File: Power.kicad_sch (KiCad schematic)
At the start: 28 parts, among them U2 RT9013-33GB, U3 TPS54560DDAR

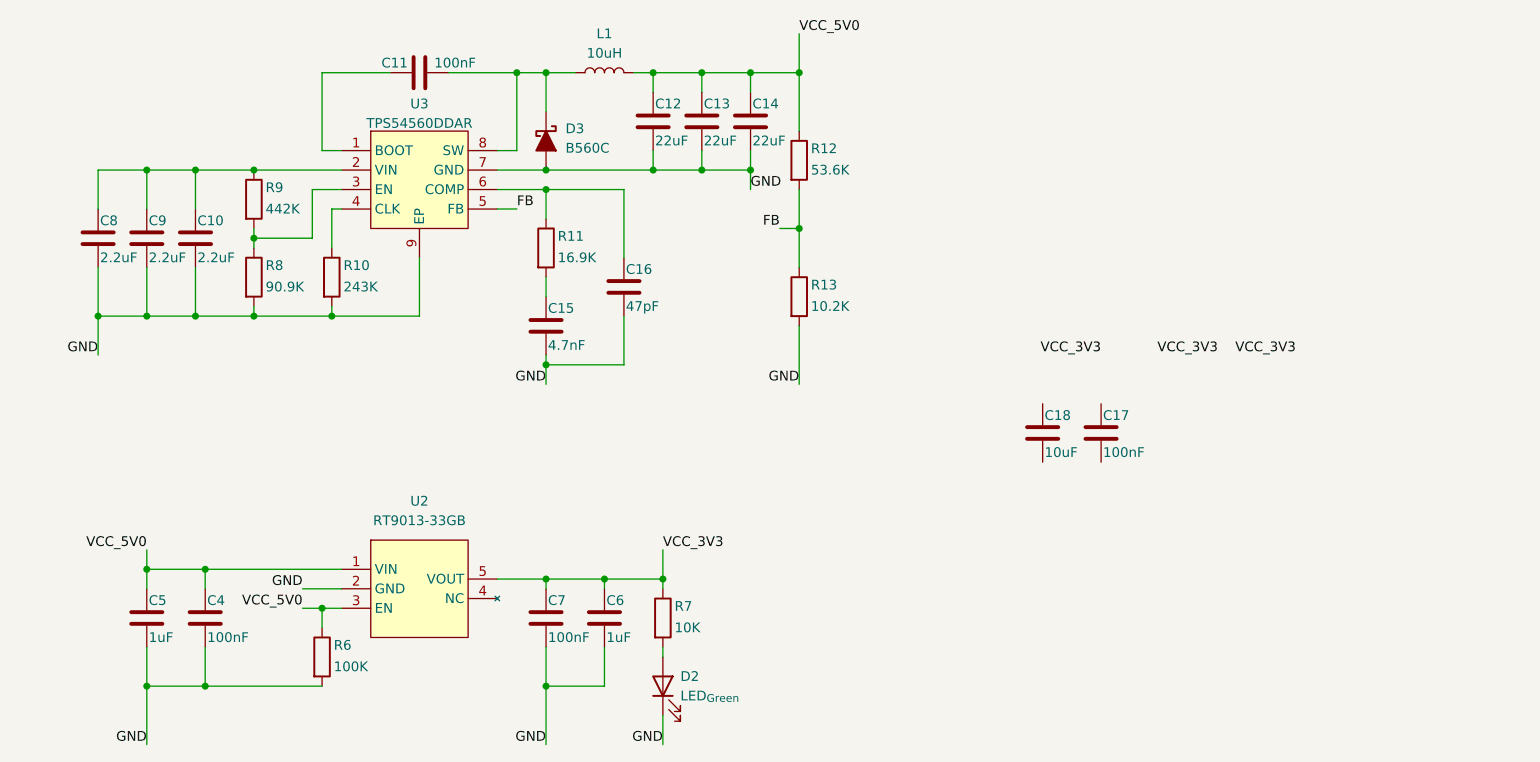
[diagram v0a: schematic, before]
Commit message: [New]: 完成整个原理图绘制和ERC检查
JIRA-ID: N/A

完成整个原理图绘制和ERC检查
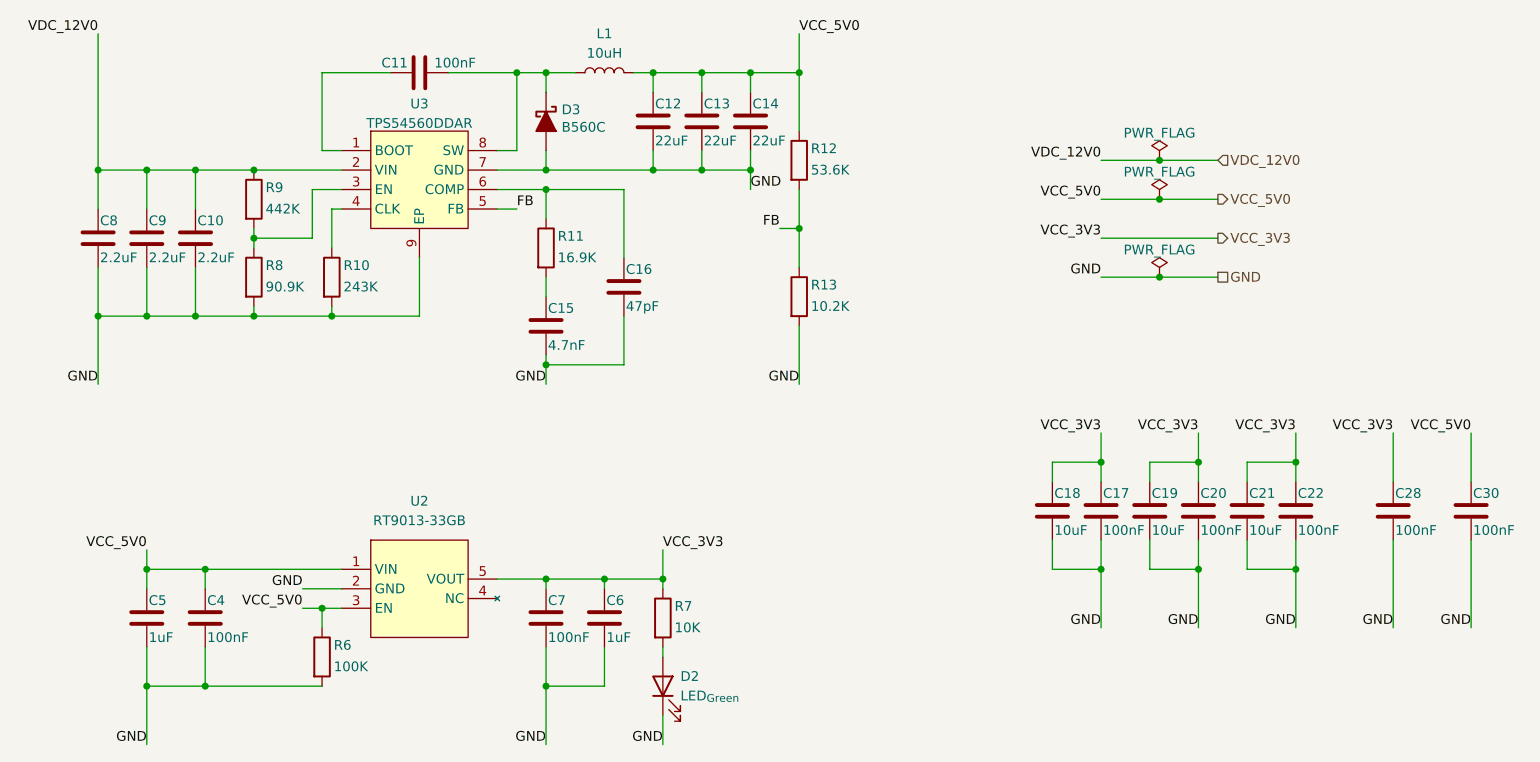
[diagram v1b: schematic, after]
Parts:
- added C19, C21: 10uF, symbol Device:C
- added C20, C22, C28, C30: 100nF, symbol Device:C
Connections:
- net GND: now also C17.2, C18.2, C19.2, C20.2, C21.2, C22.2, C28.2, C30.2
- net VCC_3V3: now also C17.1, C18.1, C19.1, C20.1, C21.1, C22.1, C28.1
- net VCC_5V0: now also C30.1
- net VDC_12V0: now reaches C10.1, C8.1, C9.1, R9.1, U3.2 (VIN)
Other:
- moved on the sheet: C17, C18, D3

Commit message: [Modify]: 完成封装的分配和PCB更新
JIRA-ID: N/A

完成封装的分配和从原理图到PCB的初始更新;完成DRC检查
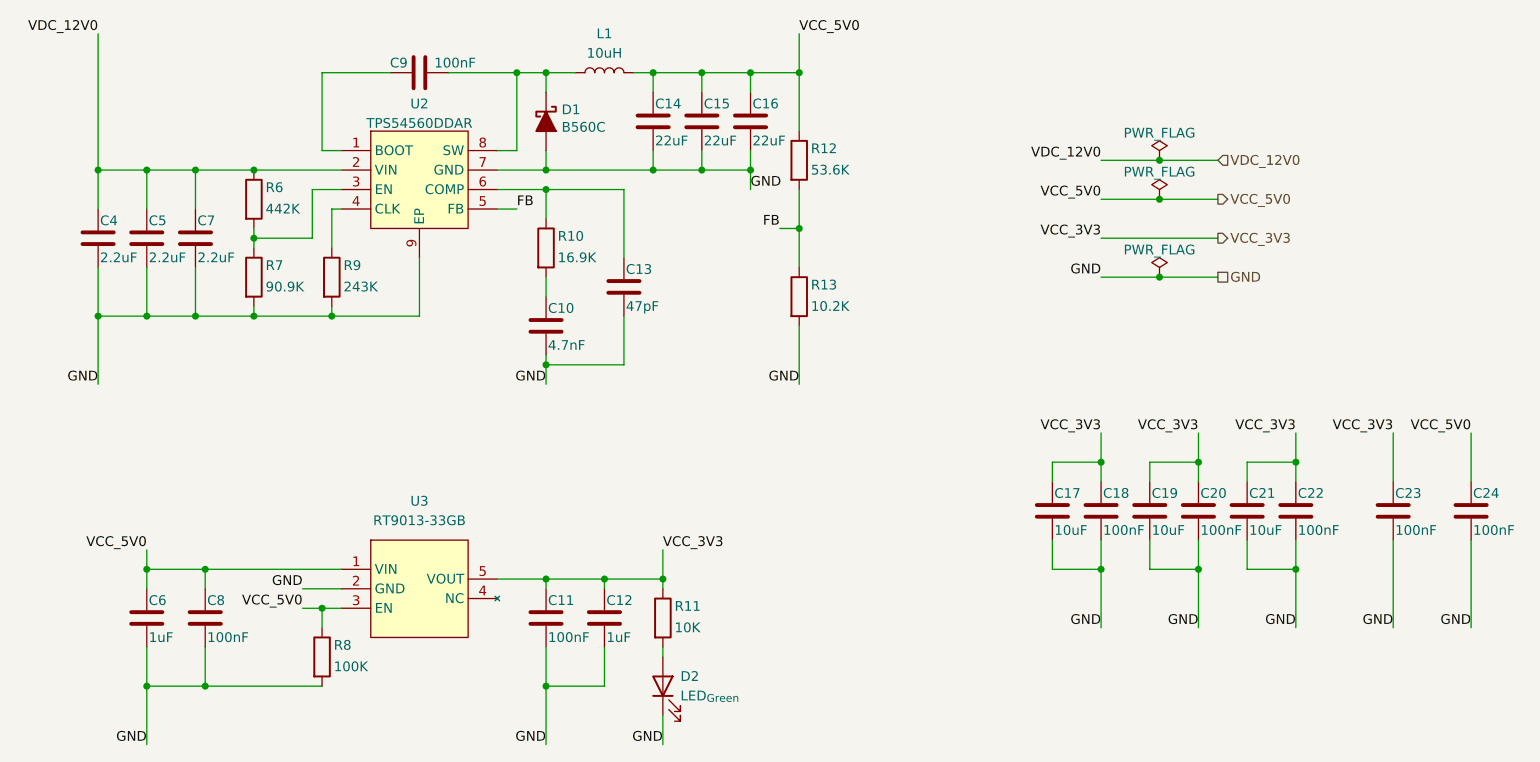
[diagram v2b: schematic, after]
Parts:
- C10: renamed from C15; footprint (none) -> Capacitor_SMD:C_0603_1608Metric
- C11: renamed from C7; footprint (none) -> Capacitor_SMD:C_0603_1608Metric
- C12: renamed from C6; footprint (none) -> Capacitor_SMD:C_0603_1608Metric
- C13: renamed from C16; footprint (none) -> Capacitor_SMD:C_0603_1608Metric
- C14: renamed from C12; footprint (none) -> Capacitor_SMD:C_0805_2012Metric
- C15: renamed from C13; footprint (none) -> Capacitor_SMD:C_0805_2012Metric
- C16: renamed from C14; footprint (none) -> Capacitor_SMD:C_0805_2012Metric
- C17: renamed from C18; footprint (none) -> Capacitor_SMD:C_0603_1608Metric
- C18: renamed from C17; footprint (none) -> Capacitor_SMD:C_0603_1608Metric
- C19, C20, C21, C22: footprint (none) -> Capacitor_SMD:C_0603_1608Metric
- C23: renamed from C28; footprint (none) -> Capacitor_SMD:C_0603_1608Metric
- C24: renamed from C30; footprint (none) -> Capacitor_SMD:C_0603_1608Metric
- C4: renamed from C8; footprint (none) -> Capacitor_SMD:C_0805_2012Metric
- C5: renamed from C9; footprint (none) -> Capacitor_SMD:C_0805_2012Metric
- C6: renamed from C5; footprint (none) -> Capacitor_SMD:C_0603_1608Metric
- C7: renamed from C10; footprint (none) -> Capacitor_SMD:C_0805_2012Metric
- C8: renamed from C4; footprint (none) -> Capacitor_SMD:C_0603_1608Metric
- C9: renamed from C11; footprint (none) -> Capacitor_SMD:C_0603_1608Metric
- D1: renamed from D3; footprint (none) -> Diode_SMD:D_SMC
- D2: footprint (none) -> LED_SMD:LED_0603_1608Metric
- L1: footprint (none) -> lidar_camera_sync:SPM7054VT-100M-D
- R10: renamed from R11; footprint (none) -> Resistor_SMD:R_0603_1608Metric
- R11: renamed from R7; footprint (none) -> Resistor_SMD:R_0603_1608Metric
- R12, R13: footprint (none) -> Resistor_SMD:R_0603_1608Metric
- R6: renamed from R9; footprint (none) -> Resistor_SMD:R_0603_1608Metric
- R7: renamed from R8; footprint (none) -> Resistor_SMD:R_0603_1608Metric
- R8: renamed from R6; footprint (none) -> Resistor_SMD:R_0603_1608Metric
- R9: renamed from R10; footprint (none) -> Resistor_SMD:R_0603_1608Metric
- U2: renamed from U3; footprint (none) -> lidar_camera_sync:SOIC8-4.9x5.4_P1.27
- U3: renamed from U2; footprint (none) -> lidar_camera_sync:SOT-23-5

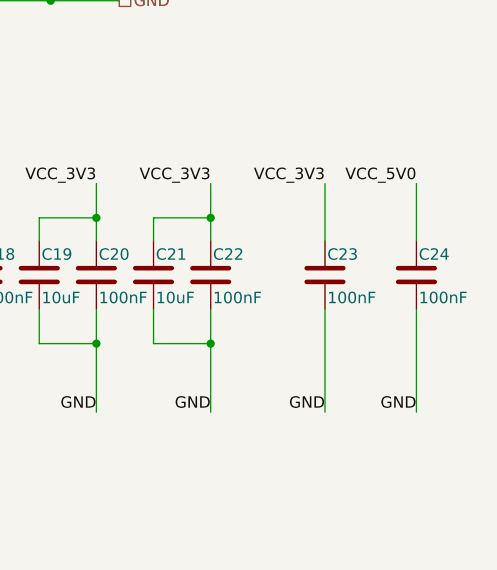
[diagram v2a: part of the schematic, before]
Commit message: [Modify]: 添加输入输出去耦电容以及WS2812B灯珠
JIRA-ID: N/A

添加输入输出去耦电容以及WS2812B灯珠
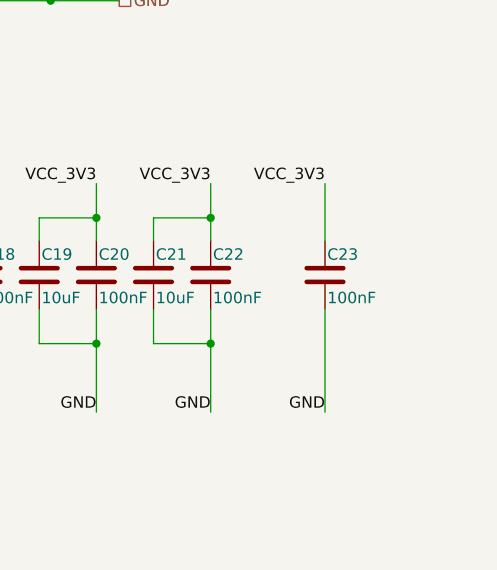
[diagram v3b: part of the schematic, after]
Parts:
- removed C24: 100nF, Capacitor_SMD:C_0603_1608Metric, symbol Device:C
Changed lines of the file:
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@@
 	(wire
 		(pts
-			(xy 264.16 109.22) (xy 264.16 115.57)
-		)
-		(stroke
-			(width 0)
-			(type default)
-		)
-	)
-	(wire
-		(pts
 			(xy 222.25 113.03) (xy 228.6 113.03)
 		)
@@
 	(wire
 		(pts
-			(xy 264.16 123.19) (xy 264.16 134.62)
-		)
-		(stroke
-			(width 0)
-			(type default)
-		)
-	)
-	(wire
-		(pts
 			(xy 176.53 95.25) (xy 176.53 102.87)
 		)
@@
 		)
 	)
-	(label "GND"
-		(at 264.16 134.62 180)
-		(effects
-			(font
-				(size 1.27 1.27)
-			)
-			(justify right bottom)
-		)
-	)
 	(label "VCC_5V0"
 		(at 176.53 57.15 0)
@@
 	)
 	(label "VCC_5V0"
-		(at 264.16 109.22 180)
-		(effects
-			(font
-				(size 1.27 1.27)
-			)
-			(justify right bottom)
-		)
-	)
-	(label "VCC_5V0"
 		(at 215.9 78.74 180)
 		(effects
@@
 					(unit 1)
 				)
-			)
-		)
-	)
-	(symbol
-		(lib_id "Device:C")
-		(at 264.16 119.38 0)
-		(unit 1)
-		(exclude_from_sim no)
-		(in_bom yes)
-		(on_board yes)
-		(dnp no)
-		(property "Reference" "C24"
-			(at 264.414 117.094 0)
-			(effects
-				(font
-					(size 1.27 1.27)
-				)
-				(justify left)
-			)
-		)
-		(property "Value" "100nF"
-			(at 264.414 121.92 0)
-			(effects
-				(font
-					(size 1.27 1.27)
-				)
-				(justify left)
-			)
-		)
-		(property "Footprint" "Capacitor_SMD:C_0603_1608Metric"
-			(at 265.1252 123.19 0)
-			(effects
-				(font
-					(size 1.27 1.27)
-				)
-				(hide yes)
-			)
-		)
-		(property "Datasheet" "~"
-			(at 264.16 119.38 0)
-			(effects
-				(font
-					(size 1.27 1.27)
-				)
-				(hide yes)
-			)
-		)
-		(property "Description" "Unpolarized capacitor"
-			(at 264.16 119.38 0)
-			(effects
-				(font
-					(size 1.27 1.27)
-				)
-				(hide yes)
-			)
-		)
-		(pin "2"
-		)
-		(pin "1"
-		)
-		(instances
-			(project "lidar_camera_sync"
-				(path "/4d41fa76-12ab-4867-bf30-96d46704f2ab/0b6b94a8-cd2e-4bd4-bd71-15c1d3af12a3"
-					(reference "C24")
-					(unit 1)
-				)
